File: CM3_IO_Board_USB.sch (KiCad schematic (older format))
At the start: 6 parts, among them U1 FE1.1s, Y1 12MHz

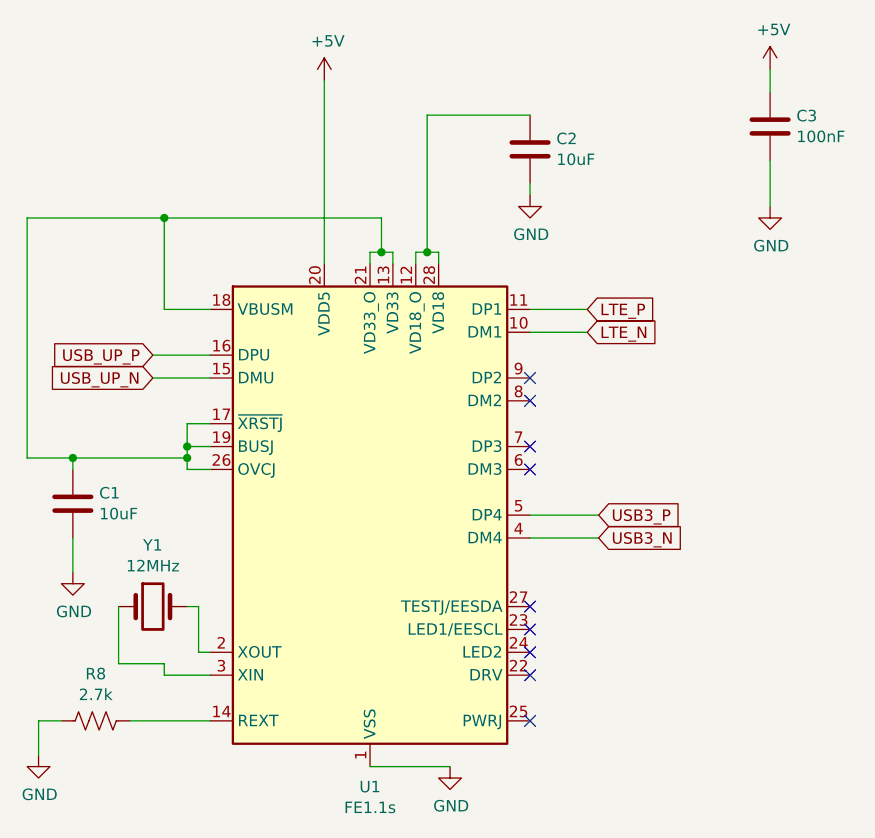
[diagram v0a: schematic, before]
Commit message: USB pinHeader added
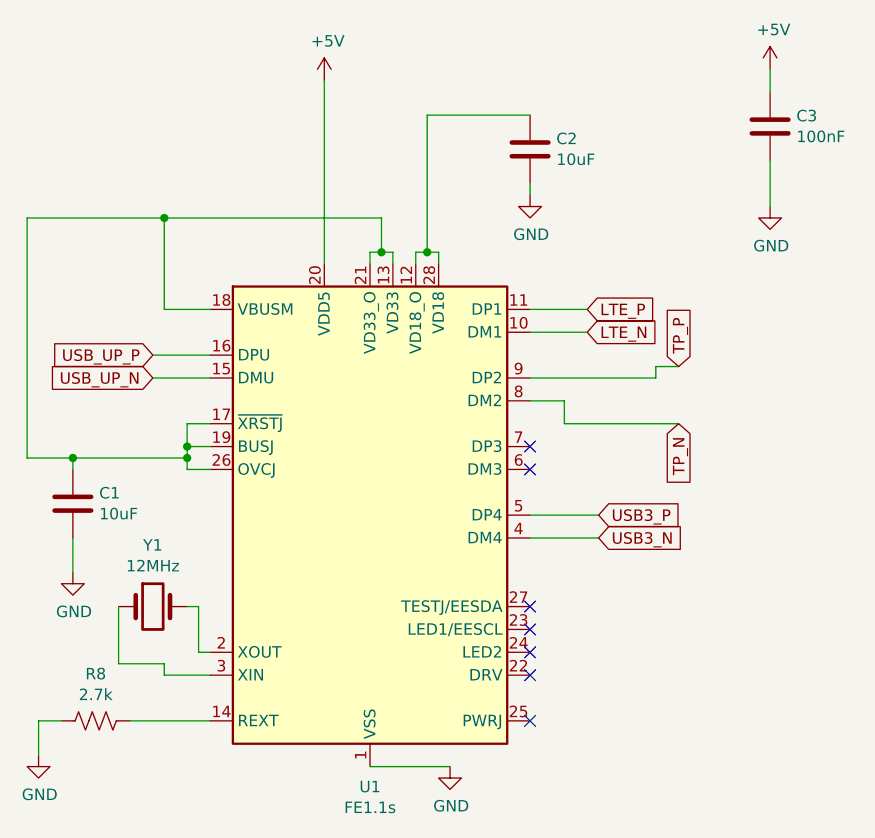
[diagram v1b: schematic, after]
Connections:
- net TP_N: now reaches U1.8 (DM2)
- net TP_P: now reaches U1.9 (DP2)
- no-connect marks 9 -> 7
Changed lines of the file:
@@
 Comment4 ""
 $EndDescr
-$Comp
-L Interface_USB:FE1.1s U1
-U 1 1 629EF2F5
-P 4750 3000
-F 0 "U1" H 4750 1811 50  0000 C CNN
-F 1 "FE1.1s" H 4750 1720 50  0000 C CNN
-F 2 "Package_SO:SSOP-28_3.9x9.9mm_P0.635mm" H 5800 1500 50  0001 C CNN
-F 3 "https://cdn-shop.adafruit.com/product-files/2991/FE1.1s+Data+Sheet+(Rev.+1.0).pdf" H 4750 3000 50  0001 C CNN
-	1    4750 3000
-	1    0    0    -1
-$EndComp
 Wire Wire Line
 	3800 2300 4050 2300
@@
 	1    0    0    -1
 $EndComp
-NoConn ~ 5450 2400
-NoConn ~ 5450 2500
 NoConn ~ 5450 2700
 NoConn ~ 5450 2800
+$Comp
+L Interface_USB:FE1.1s U1
+U 1 1 629EF2F5
+P 4750 3000
+F 0 "U1" H 4750 1811 50  0000 C CNN
+F 1 "FE1.1s" H 4750 1720 50  0000 C CNN
+F 2 "Package_SO:SSOP-28_3.9x9.9mm_P0.635mm" H 5800 1500 50  0001 C CNN
+F 3 "https://cdn-shop.adafruit.com/product-files/2991/FE1.1s+Data+Sheet+(Rev.+1.0).pdf" H 4750 3000 50  0001 C CNN
+	1    4750 3000
+	1    0    0    -1
+$EndComp
+Wire Wire Line
+	6100 2600 5600 2600
+Wire Wire Line
+	5600 2600 5600 2500
+Wire Wire Line
+	5600 2500 5450 2500
+Wire Wire Line
+	5450 2400 6000 2400
+Wire Wire Line
+	6000 2400 6000 2350
+Wire Wire Line
+	6000 2350 6100 2350
+Text GLabel 6100 2350 1    50   Input ~ 0
+TP_P
+Text GLabel 6100 2600 3    50   Input ~ 0
+TP_N
 $EndSCHEMATC
